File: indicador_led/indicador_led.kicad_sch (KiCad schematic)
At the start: 3 parts, among them J1 Conn_01x02_Pin

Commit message: fix
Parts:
- R1: value R -> 3k
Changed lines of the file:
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@@
 			)
 		)
-		(property "Value" "R"
+		(property "Value" "3k"
 			(at 107.95 102.8699 0)
 			(show_name no)

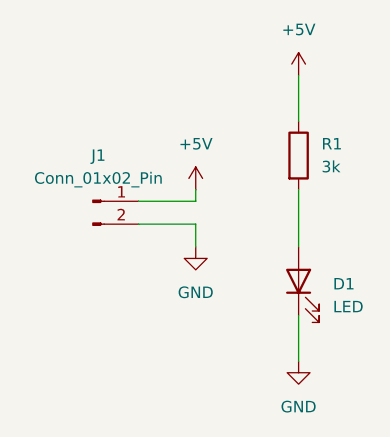
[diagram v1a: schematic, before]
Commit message: fix: altere R1 de 35k para 3k
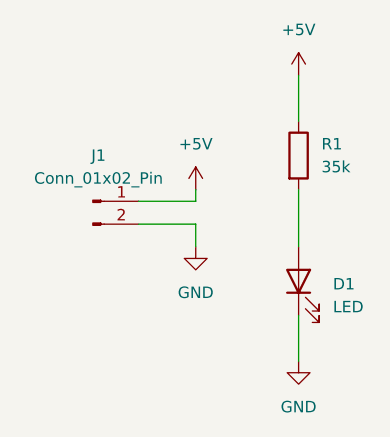
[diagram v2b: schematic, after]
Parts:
- R1: value 3k -> 35k
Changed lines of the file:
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@@
 			)
 		)
-		(property "Value" "3k"
+		(property "Value" "35k"
 			(at 107.95 102.8699 0)
 			(show_name no)
